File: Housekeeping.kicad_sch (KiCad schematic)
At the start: 98 parts, among them J5 PPS IN, J6 WP Jumper, Q1 FDN335N, Q2 FDN335N, U123 MAX4896, U15 AT24C64D, U16 SI5330B-B00206-GM, U19 74AVC4T245, U36 TL071H, U37 TXU0101

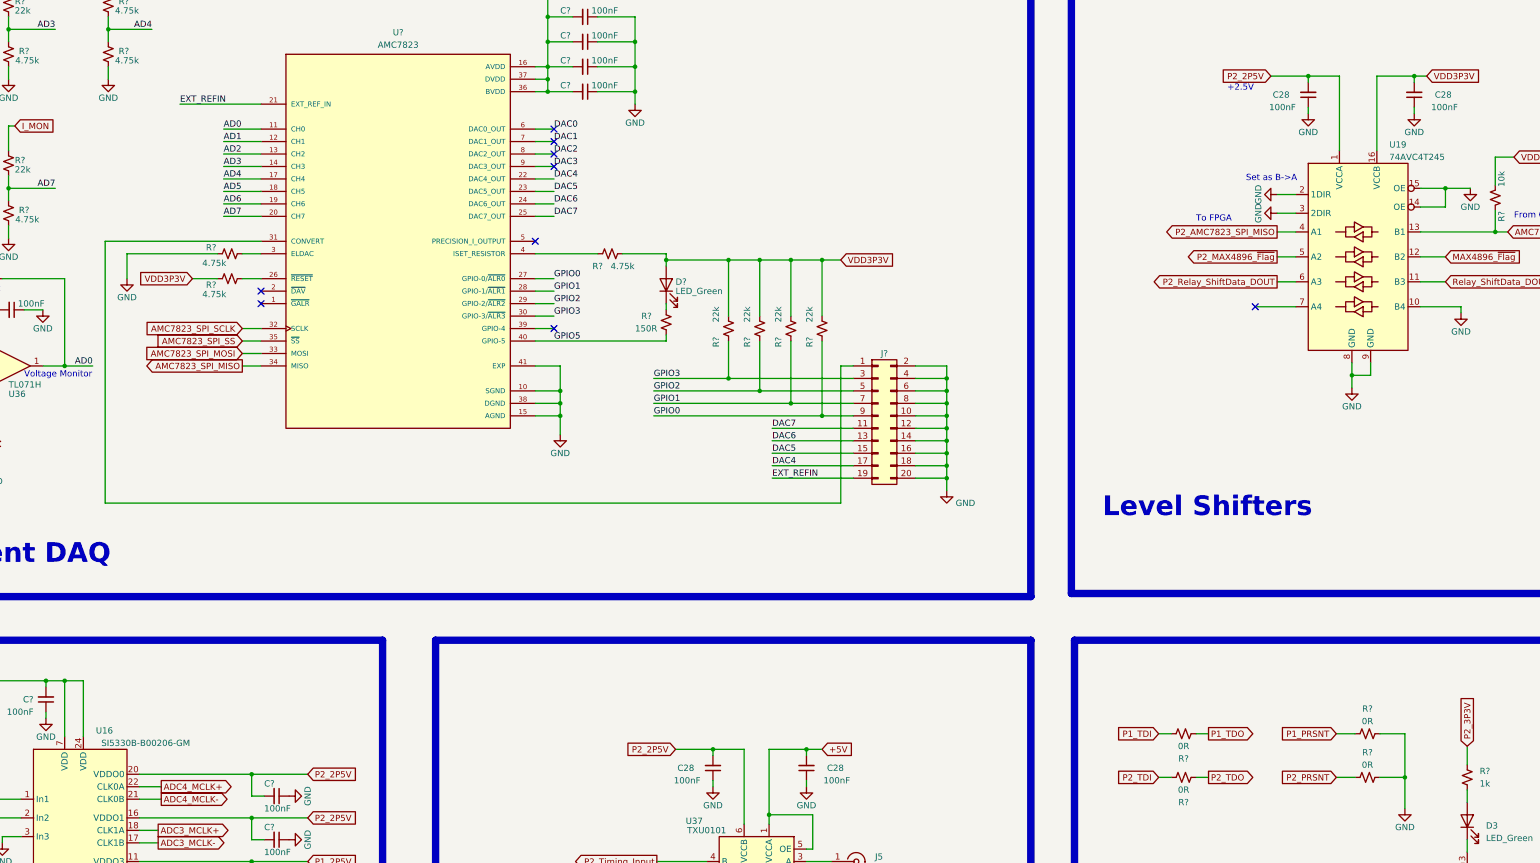
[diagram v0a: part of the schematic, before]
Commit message: Updating design to cover reworks
Updating design to cover reworks.
This should now match what has been delivered to NASA GRE-ATF after the board reworks.
All outputs have been regenerated
Changes are:
1)Changed the clock splitter part to a 2.5V compatible part
2)Changed some caps on the MCLK lines to 0R resitors
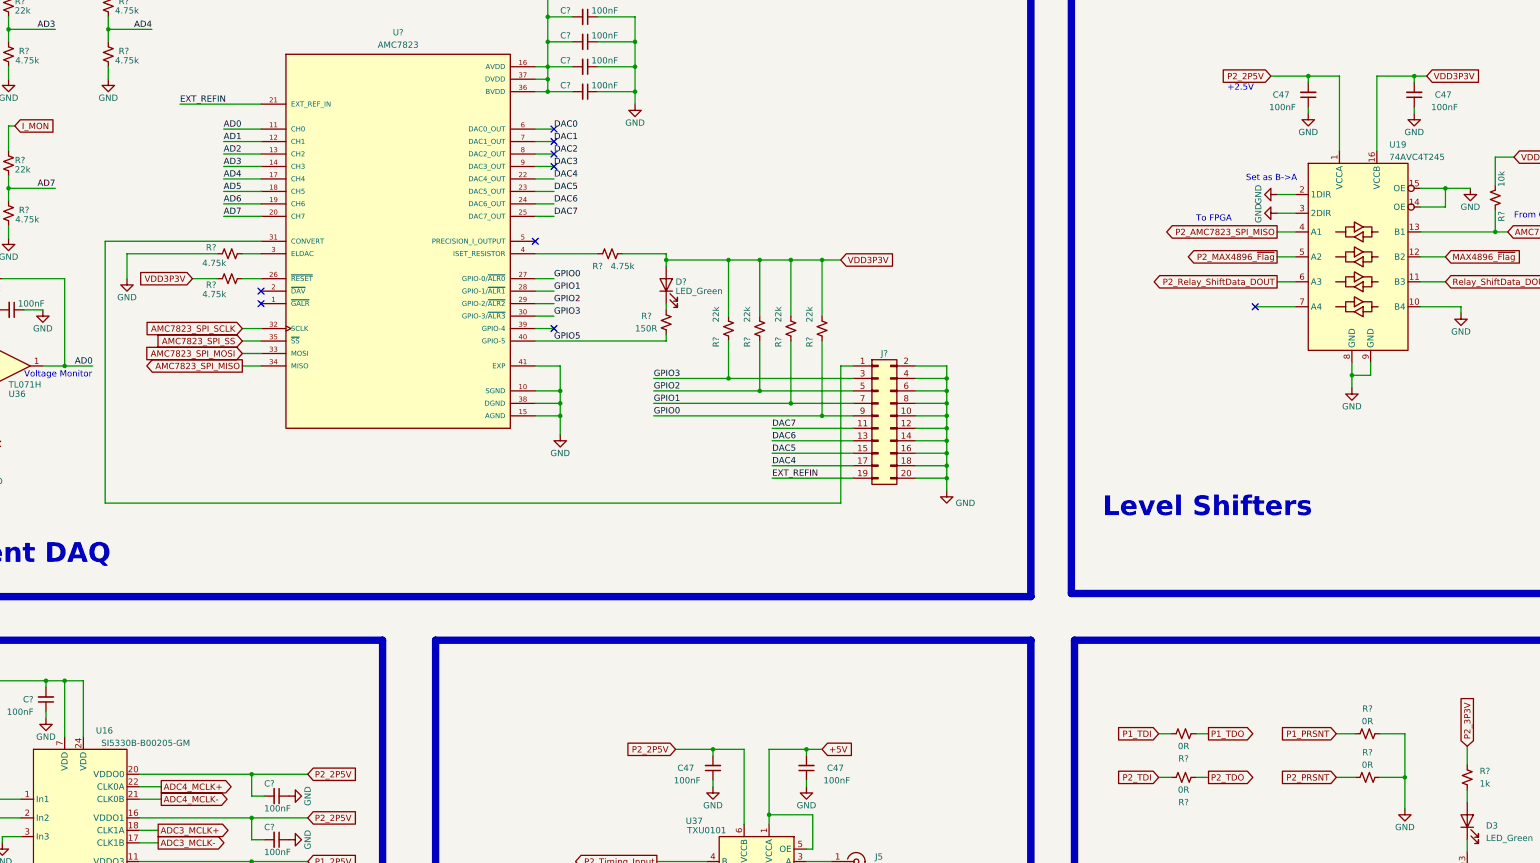
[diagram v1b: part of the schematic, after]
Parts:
- U16: value SI5330B-B00206-GM -> SI5330B-B00205-GM; MPN SI5330B-B00206-GM -> SI5330B-B00205-GM
- renumbered C28 to C47
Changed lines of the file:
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@@
 		(on_board yes)
 		(dnp no)
-		(property "Reference" "#PWR030"
+		(property "Reference" "#PWR063"
 			(at 367.665 78.105 0)
 			(effects
@@
 		(on_board yes)
 		(dnp no)
-		(property "Reference" "#PWR030"
+		(property "Reference" "#PWR063"
 			(at 365.76 103.505 0)
 			(effects
@@
 		(on_board yes)
 		(dnp no)
-		(property "Reference" "#PWR030"
+		(property "Reference" "#PWR063"
 			(at 334.645 62.865 0)
 			(effects
@@
 		(on_board yes)
 		(dnp no)
-		(property "Reference" "#PWR030"
+		(property "Reference" "#PWR063"
 			(at 343.535 118.745 0)
 			(effects
@@
 		(on_board yes)
 		(dnp no)
-		(property "Reference" "C28"
+		(property "Reference" "C47"
 			(at 363.855 52.705 0)
 			(effects
@@
 			)
 		)
-		(property "Datasheet" " ~"
+		(property "Datasheet" "~"
 			(at 242.57 208.915 0)
 			(effects
@@
 		(on_board yes)
 		(dnp no)
-		(property "Reference" "#PWR030"
+		(property "Reference" "#PWR063"
 			(at 213.36 200.025 0)
 			(effects
@@
 		(on_board yes)
 		(dnp no)
-		(property "Reference" "#PWR030"
+		(property "Reference" "#PWR063"
 			(at 242.57 227.965 0)
 			(effects
@@
 		(on_board yes)
 		(dnp no)
-		(property "Reference" "#PWR030"
+		(property "Reference" "#PWR063"
 			(at 222.25 225.425 0)
 			(effects
@@
 		(on_board yes)
 		(dnp no)
-		(property "Reference" "#PWR030"
+		(property "Reference" "#PWR063"
 			(at 321.945 73.025 0)
 			(effects
@@
 		(on_board yes)
 		(dnp no)
-		(property "Reference" "C28"
+		(property "Reference" "C47"
 			(at 330.835 52.705 0)
 			(effects
@@
 			)
 		)
-		(property "Value" "SI5330B-B00206-GM"
+		(property "Value" "SI5330B-B00205-GM"
 			(at 97.79 184.785 0)
 			(effects
@@
 			)
 		)
-		(property "MPN" "SI5330B-B00206-GM"
+		(property "MPN" "SI5330B-B00205-GM"
 			(at 74.93 186.055 0)
 			(effects
@@
 		(on_board yes)
 		(dnp no)
-		(property "Reference" "#PWR030"
+		(property "Reference" "#PWR063"
 			(at 437.515 84.455 0)
 			(effects
@@
 		(on_board yes)
 		(dnp no)
-		(property "Reference" "C28"
+		(property "Reference" "C47"
 			(at 240.03 189.865 0)
 			(effects
@@
 		(on_board yes)
 		(dnp no)
-		(property "Reference" "#PWR030"
+		(property "Reference" "#PWR063"
 			(at 321.945 76.835 0)
 			(effects
@@
 		(on_board yes)
 		(dnp no)
-		(property "Reference" "#PWR030"
+		(property "Reference" "#PWR063"
 			(at 232.41 200.025 0)
 			(effects
@@
 		(on_board yes)
 		(dnp no)
-		(property "Reference" "#PWR030"
+		(property "Reference" "#PWR063"
 			(at 356.235 62.865 0)
 			(effects
@@
 		(on_board yes)
 		(dnp no)
-		(property "Reference" "C28"
+		(property "Reference" "C47"
 			(at 209.55 189.865 0)
 			(effects

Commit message: Opened & Saved Project in Kicad 9
- Opened & Saved Project in Kicad 9
- Added .gitignore from main
- Added sym-lib-table to link the unchanged symbol libs to the project
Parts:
- gave numbers to parts that had none: 68
- renumbered C47 to C123, C47 to C124, C47 to C130, C47 to C133, D3 to D2, H2 to H3, R18 to R35, R18 to R43, U123 to U14, U123 to U15, U123 to U17, U123 to U18, U123 to U19, U123 to U20, U123 to U21, U123 to U23, U19 to U26, U15 to U27

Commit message: Updated and Condensed Project Symbol Libraries
- Added Symbols for part used in main(Quartz v2 branch)
  -ADM1185
  -TPS275
  -TPS561208

- Removed outdated/unused Symbol libraries
  - max4896 (project already copied contents to AD7768_Digitizer_SLib)
  - AD7768_Digitizer_SLibv2 (No links were made to this library under the current project)

- Fixed Symbol Library Links on
  - U13 (Was pointing to AMC7823 lib; saved copy of part in AD7768_Digitizer_SLib & relinked)
  - U26 (Was pointing to Custom_Zest lib; saved copy of part in AD7768_Digitizer_SLib & relinked)
  - U29 (Was pointing to Custom_Zest lib; saved copy of part in AD7768_Digitizer_SLib & relinked)

- Relinked P1 & P2
  Somehow this was in the schematic but not in AD7768_Digitizer_SLib although it was linked to that lib.
  A copy was made and added to AD7768_Digitizer_SLib from the main branch, where the part exists.
  No change to the part seems to have occured in the schematic.

- Changed sym-lib-table to just point to the now one project symbol library
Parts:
- U13: symbol AMC7823IRTAR:AMC7823IRTAR -> AD7768_Digitizer_SLib:AMC7823IRTAR
- U26: symbol Custom_Lib_MPEX_Zest:74LVC4T245 -> AD7768_Digitizer_SLib:74LVC4T245
- U29: symbol Custom_Lib_MPEX_Zest:74LVC8T245 -> AD7768_Digitizer_SLib:74LVC8T245
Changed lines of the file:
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@@
 	)
 	(symbol
-		(lib_id "Custom_Lib_MPEX_Zest:74LVC4T245")
+		(lib_id "AD7768_Digitizer_SLib:74LVC4T245")
 		(at 334.645 66.675 0)
 		(unit 1)
@@
 	)
 	(symbol
-		(lib_id "Custom_Lib_MPEX_Zest:74LVC8T245")
+		(lib_id "AD7768_Digitizer_SLib:74LVC8T245")
 		(at 449.58 51.435 0)
 		(unit 1)
@@
 	)
 	(symbol
-		(lib_id "AMC7823IRTAR:AMC7823IRTAR")
+		(lib_id "AD7768_Digitizer_SLib:AMC7823IRTAR")
 		(at 120.015 72.39 0)
 		(unit 1)

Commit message: Fixed Serveral ERC errors
Fixed Several ERC errors
- Ignored off-grid connections errors

- Updated a number of symbols from the Kicad default library. This should have no visual change
  - Power:Ground
  - Power:Earth
  - Device:LED

- Relinked some symbols with a new copy in the AD7688_Digitaizer_SLib. This was to fix errors/warnings where local schematic changes were made. This process was opening the local symbol; saving a copy in the AD7688_Digitaizer_SLib; relinking the part to the new part in the AD7688_Digitaizer_SLib. This should have caused no visual change.
  - EC2-12TNU relays parts (K101 etc.)
  - U36 TL071
  - U16 SI5330 (had local edit to add pin25-gnd pad)
  - U32 TXU101

- Changed D4 symbol to explicitly show the unused pin on the schematic (was an error)

- Removed an extra pin 25 from U35 showing the pad connection. Renamed the pin for clarity
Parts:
- U36: symbol Amplifier_Operational:TL071 -> AD7768_Digitizer_SLib:TL071
- U37: symbol Logic_LevelTranslator:SN74AUP1T34DCK -> AD7768_Digitizer_SLib:TXU0101
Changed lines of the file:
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@@
 	)
 	(symbol
-		(lib_id "Amplifier_Operational:TL071")
+		(lib_id "AD7768_Digitizer_SLib:TL071")
 		(at 69.215 107.95 0)
 		(mirror x)
@@
 	)
 	(symbol
-		(lib_id "Logic_LevelTranslator:SN74AUP1T34DCK")
+		(lib_id "AD7768_Digitizer_SLib:TXU0101")
 		(at 222.25 208.915 0)
 		(mirror y)

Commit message: Fixed remaining ERC errors and Warnings
No changes affecting copper were made.
At the end of this commits changes all changes from this and the previous two commits were pulled into the PCB.
No changes to the layout occurred and no additional pcb error or warning were made

Detailed Changes:
-Saved the Local Symbol to the project symbol lib and relinked for
  - Q1 & Q2 (looks like symbol was removed from std lib)
  - Max4896 IC's (U14..U23)
  - U32 | ZXCT1009F
  - L8 | MDS1260
  - Q3
  - U33
  - U34 to include thermal pad definitions
  - Mounting holes (Caused a footprint linking error as we linked to a custom footprint)
  - L7 (Caused a footprint linking error as we linked to a custom footprint)
  - P1 & P2 FMC connectors

-Removed Footprint Filter on the following library symbols to clear the footprint linking error
  - DB37 Connectors
  - Relays
  - Mounting Holes
  - U36, U37, D4, L7, L8, U33

-Updated J5 from standard library (no visual change occurred)

-Added Power Flag directives to clear up some warning on various power rails.

-Excluded 5 remaining warnings with comments
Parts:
- H1, H2, H3: symbol Mechanical:MountingHole_Pad -> AD7768_Digitizer_SLib:MountingHole_Pad
- Q1, Q2: symbol Device:Q_NMOS_GSD -> AD7768_Digitizer_SLib:Q_NMOS_GSD
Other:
- moved on the sheet: R11, R118, R119, R16, R23, R28, R29, R30, R31, R34, R47, R48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

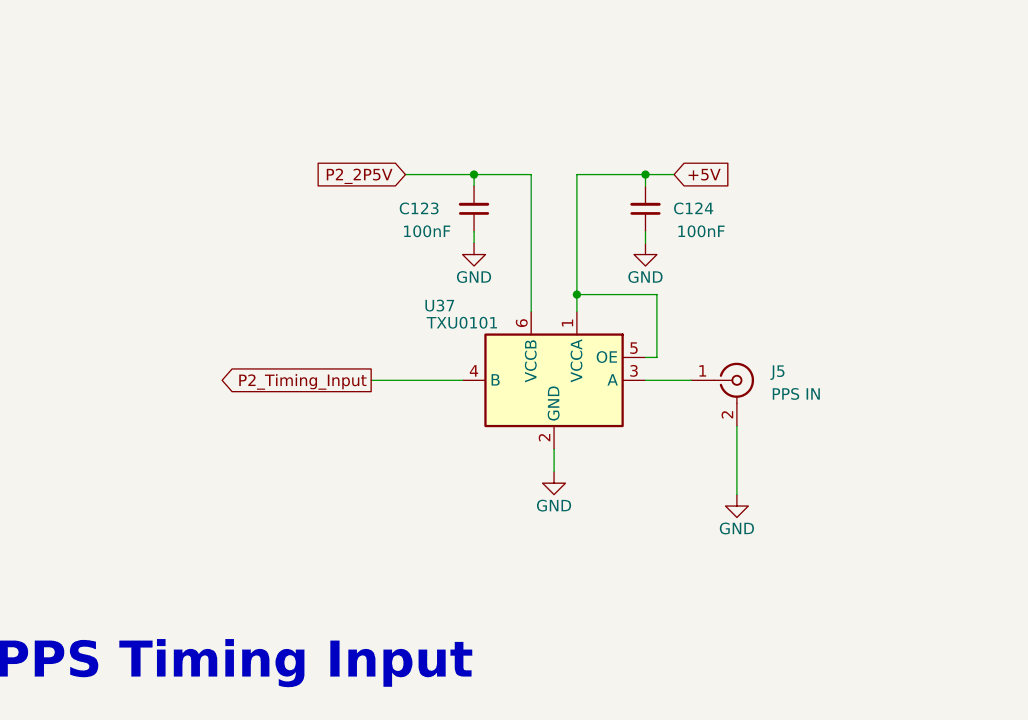
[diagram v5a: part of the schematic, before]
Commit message: Verified 'Must do changes' implemented all 'should do' changes
Must do Changes that have been verified:
-Change the Clock divider chip to the 2,5V part
-Remove AC coupling caps in clock lines

Should do changes implmented
  - Add pull up resistor to ADC reset lines
  - Internal termination of PPS (when unused)
  - Add Heat Sinking to inductors by increased traces/planes size (Copied/Based-On from V2 Design)
  - Changed to a 2.048V VREF with accompanying removal of INA851 gain resistor (this will give more dynamic range)
  - Move ground test points further away from power rails

Also Included Some Improvments to the power rails seen in V2 when in comes to:
-12V rail into the power section and up to the front of the board
-The 3.3V rail that goes around the edge of the board to the relay switch IC's

Note - DRC warnings that exist are either ignorable, or pointing to the fact that the default footprint libs may have been changed in Kicad9 causeing a mismatch to what is on the board. I will no update these footprint to the new version yet, or possibly ever.
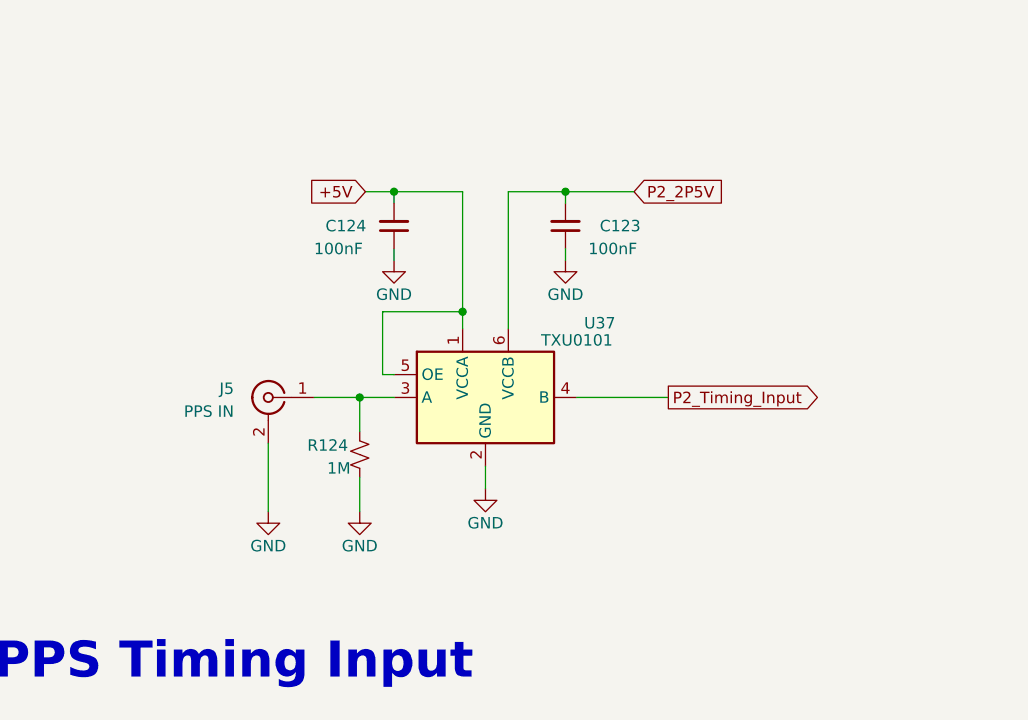
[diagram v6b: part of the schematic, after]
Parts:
- added R124: 1M, Resistor_SMD:R_0603_1608Metric, symbol Device:R_Small_US
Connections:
- net GND: now also R124.2
- net at J5.1 (In), U37.3 (A): now also R124.1
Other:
- moved on the sheet: C123, C124, J5, U37

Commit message: Added Calibration EEPROM
-Added Calibration EEPROM
-Changed WP headers to 100mil spaced part
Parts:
- added C132: 1uF, Capacitor_SMD:C_0603_1608Metric, symbol Device:C_Small
- added J7: WP Jumper, Connector_PinHeader_2.54mm:PinHeader_1x02_P2.54mm_Vertical, symbol Connector_Generic:Conn_01x02
- added R121, R122, R123, R126, R127: 4.75k, Resistor_SMD:R_0402_1005Metric, symbol Device:R_Small_US
- added R125: 11.5k, Resistor_SMD:R_0402_1005Metric, symbol Device:R_Small_US
- added U28: AT24C64D, Package_SO:SOIC-8_3.9x4.9mm_P1.27mm, symbol Memory_EEPROM:AT24CS01-SSHM
- J6: footprint Connector_PinHeader_2.00mm:PinHeader_1x02_P2.00mm_Vertical -> Connector_PinHeader_2.54mm:PinHeader_1x02_P2.54mm_Vertical; MPN M22-2510205 -> M20-9990245
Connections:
- net GND: now also C132.2, J7.2 (Pin_2), U28.4 (GND)
- net VDD3P3V: now also C132.1, R125.1, R126.1, R127.1, U28.8 (VCC)
- new net: R122.2, U28.2 (A1)
- new net: R121.2, U28.1 (A0)
- new net: J7.1 (Pin_1), R125.2, U28.7 (WP)
- new net: R123.2, U28.3 (A2)
- new net CAL_EEPROM_A0: R121.1
- new net CAL_EEPROM_A1: R122.1
- new net CAL_EEPROM_A2: R123.1
- new net CAL_EEPROM_SCL: R127.2, U28.6 (SCL)
- new net CAL_EEPROM_SDA: R126.2, U28.5 (SDA)
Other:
- note added: "CAL EEPROM"
- moved on the sheet: C116, C117, C121, C122, C126, C127, C94, C95, R43, U14, U15, U17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

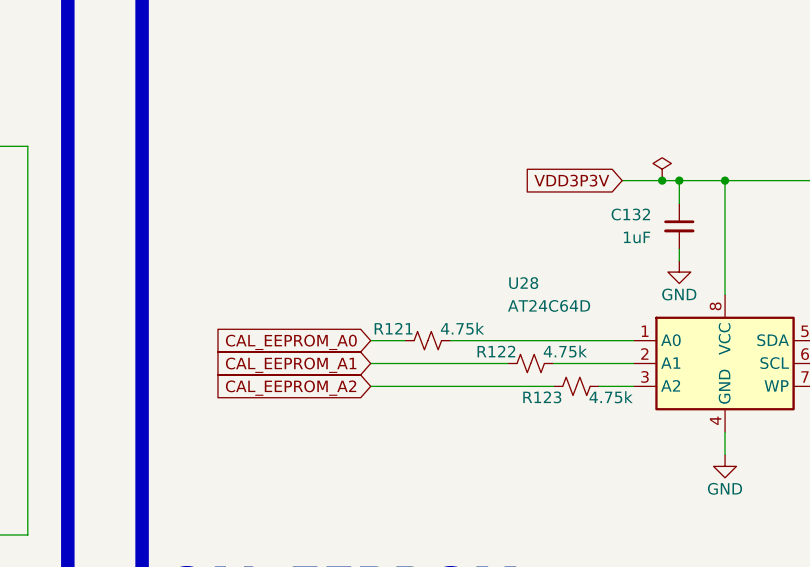
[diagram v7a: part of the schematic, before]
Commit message: Changed Cal EEPROM to run off 2.5V
Changed Cal EEPROM to run off 2.5V
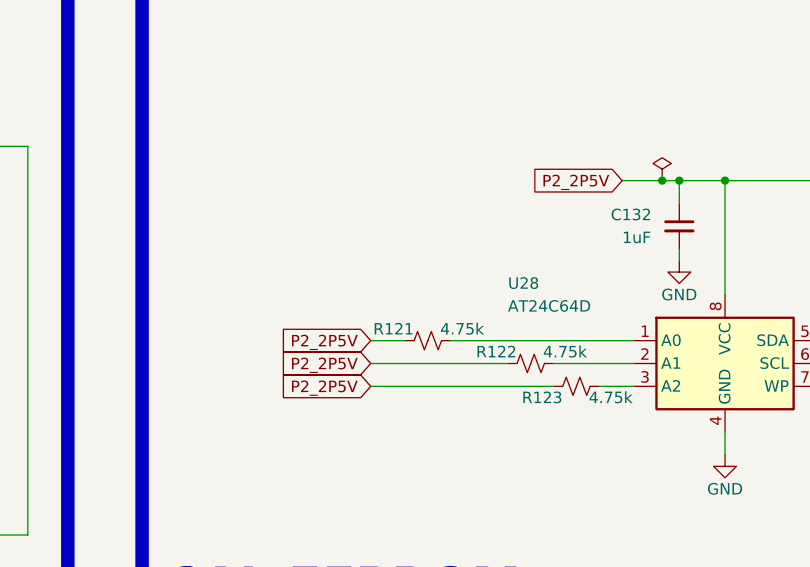
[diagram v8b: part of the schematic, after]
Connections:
- net CAL_EEPROM_A0 is gone; now on net P2_2P5V: R121.1
- net CAL_EEPROM_A1 is gone; now on net P2_2P5V: R122.1
- net CAL_EEPROM_A2 is gone; now on net P2_2P5V: R123.1
- net P2_2P5V: now also C132.1, R125.1, R126.1, R127.1, U28.8 (VCC)
- net VDD3P3V: no longer C132.1, R125.1, R126.1, R127.1, U28.8 (VCC)
